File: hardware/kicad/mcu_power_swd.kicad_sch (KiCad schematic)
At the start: 27 parts, among them J1 5V INPUT: 1=+5V 2=GND, J2 SWD: VTref IO GND CLK RST SWO, U1 STM32G431RBT6, U2 AP2112K-3.3TRG1

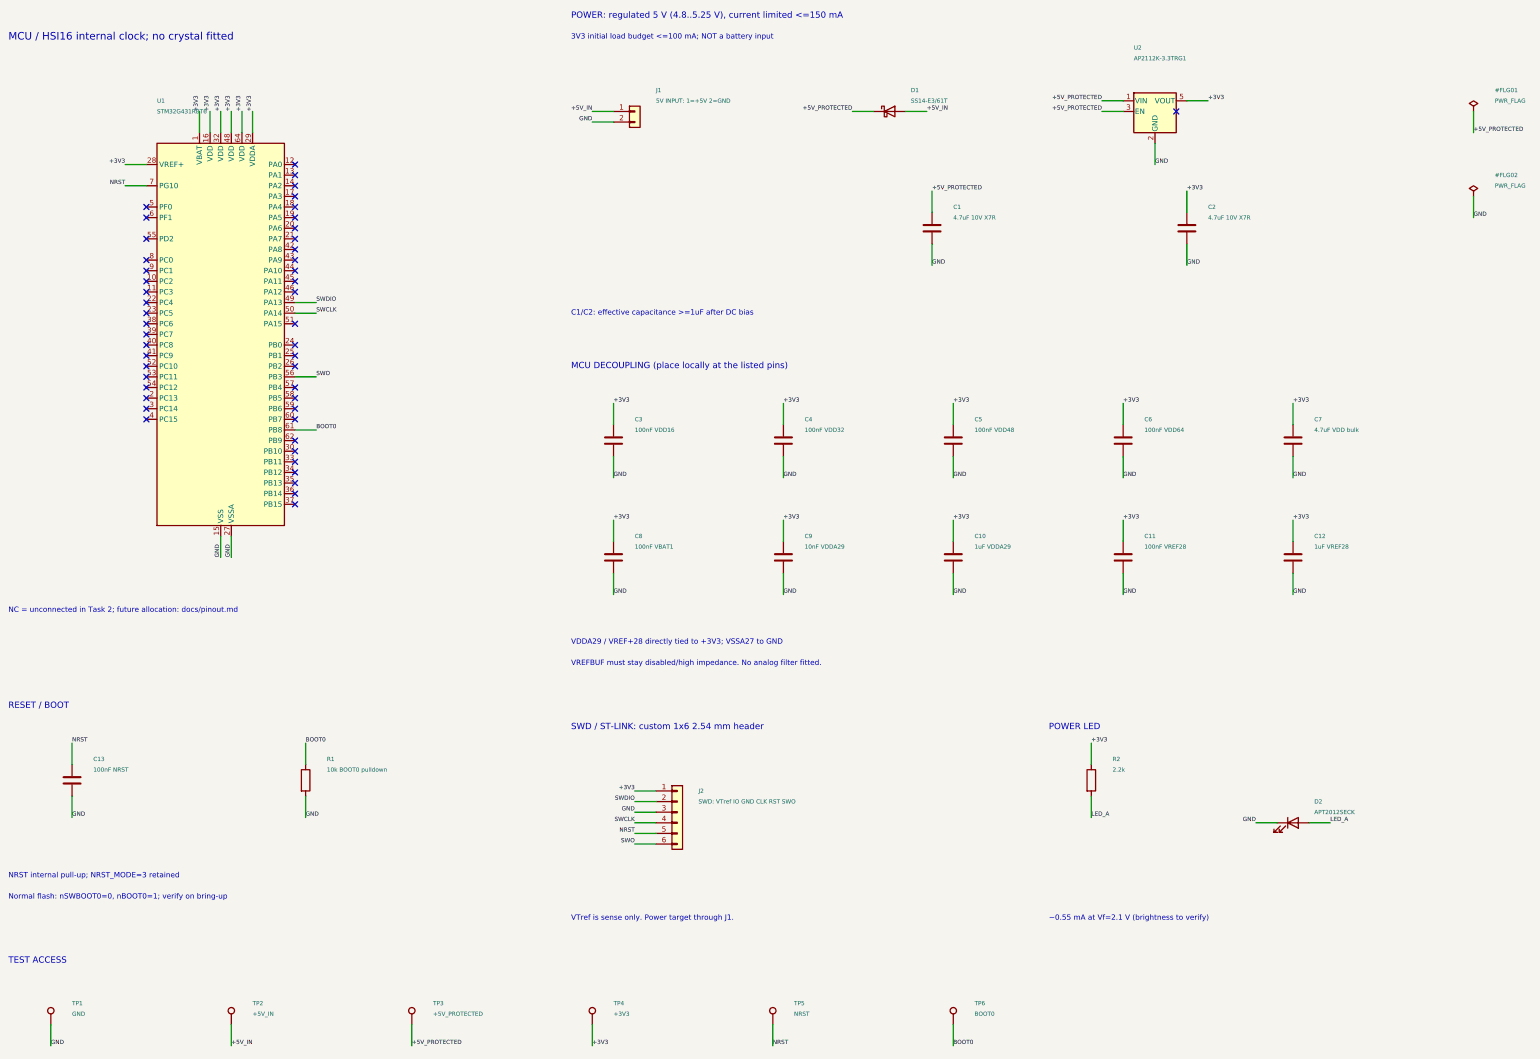
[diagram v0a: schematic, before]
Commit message: hardware: add verified CAN sensor and ESC interfaces
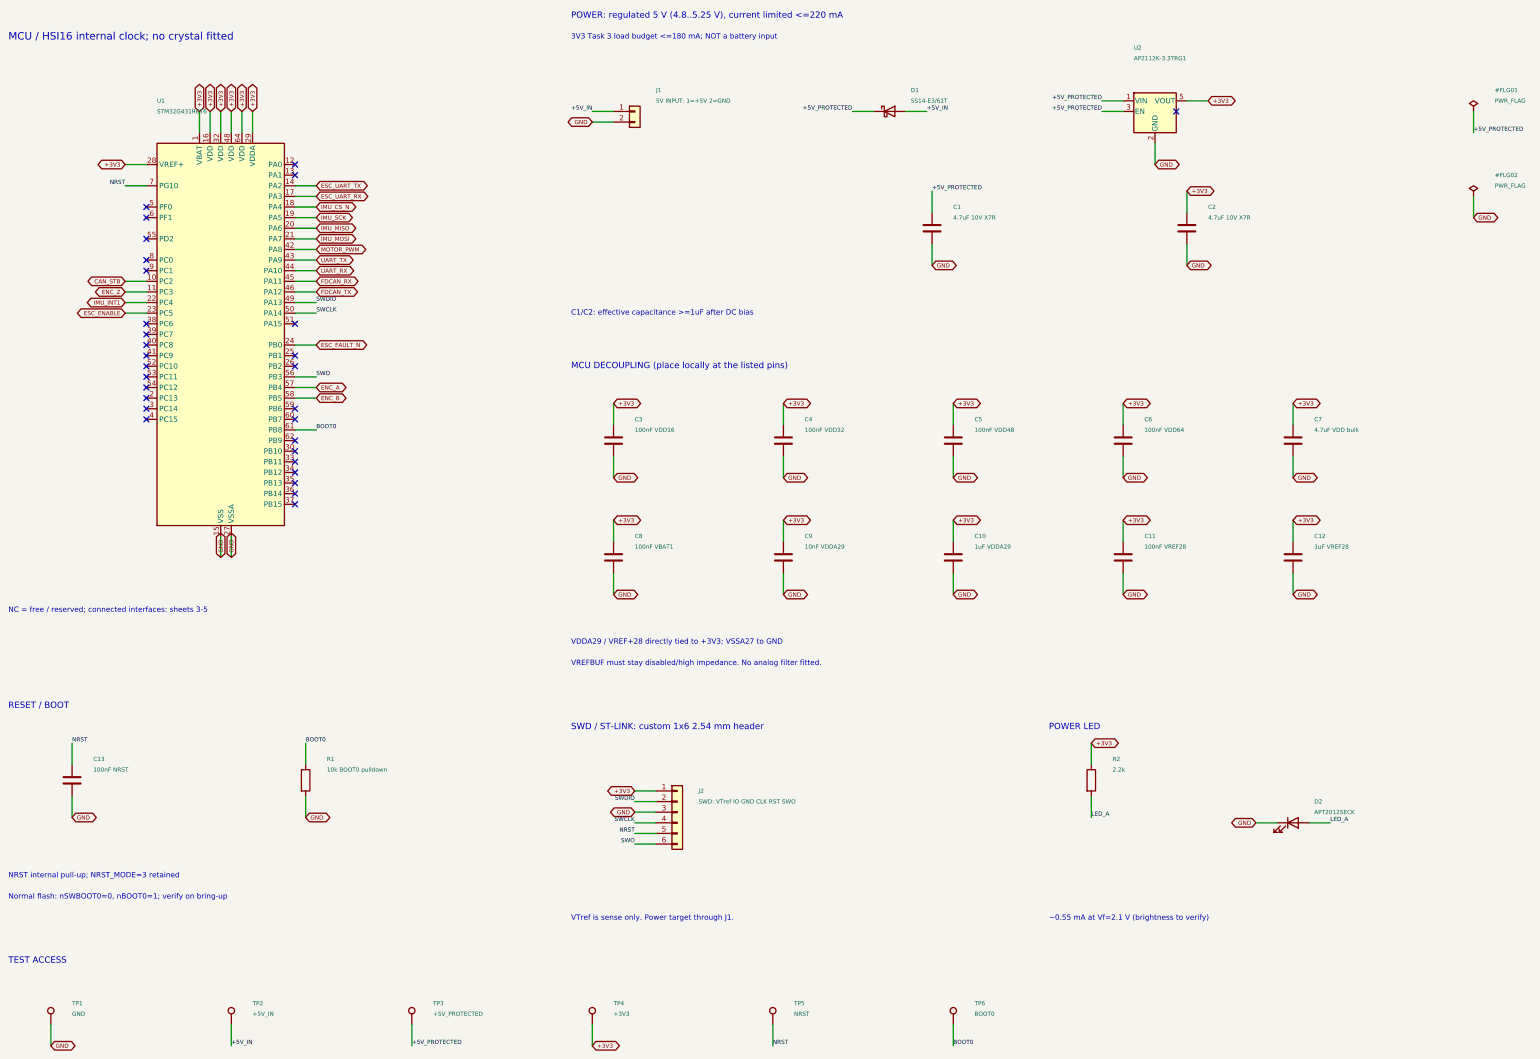
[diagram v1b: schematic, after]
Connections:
- net CAN_STB: now reaches U1.10 (PC2)
- net ENC_Z: now reaches U1.11 (PC3)
- net ESC_UART_TX: now reaches U1.14 (PA2)
- net ESC_UART_RX: now reaches U1.17 (PA3)
- net IMU_CS_N: now reaches U1.18 (PA4)
- net IMU_SCK: now reaches U1.19 (PA5)
- net IMU_MISO: now reaches U1.20 (PA6)
- net IMU_MOSI: now reaches U1.21 (PA7)
- net IMU_INT1: now reaches U1.22 (PC4)
- net ESC_ENABLE: now reaches U1.23 (PC5)
- net ESC_FAULT_N: now reaches U1.24 (PB0)
- net MOTOR_PWM: now reaches U1.42 (PA8)
- net UART_TX: now reaches U1.43 (PA9)
- net UART_RX: now reaches U1.44 (PA10)
- net FDCAN_RX: now reaches U1.45 (PA11)
- net FDCAN_TX: now reaches U1.46 (PA12)
- net ENC_A: now reaches U1.57 (PB4)
- net ENC_B: now reaches U1.58 (PB5)
- no-connect marks 48 -> 30
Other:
- note added: "3V3 Task 3 load budget <=180 mA; NOT a battery input"
- note added: "NC = free / reserved; connected interfaces: sheets 3-5"
- note added: "POWER: regulated 5 V (4.8..5.25 V), current limited <=220 mA"
- note removed: "3V3 initial load budget <=100 mA; NOT a battery input"
- note removed: "NC = unconnected in Task 2; future allocation: docs/pinout.md"
- note removed: "POWER: regulated 5 V (4.8..5.25 V), current limited <=150 mA"
- title: MCU + power + SWD - Task 2 -> MCU + power + SWD - Task 3 connections

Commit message: hardware: review schematic and align mechanical and probe attributes
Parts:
- TP1, TP2, TP3, TP4, TP5, TP6: now left out of the parts list
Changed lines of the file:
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@@
 (text "~0.55 mA at Vf=2.1 V (brightness to verify)" (at 274.32 241.3 0) (effects (font (size 1.27 1.27)) (justify left)))
 (text "TEST ACCESS" (at 25.4 251.46 0) (effects (font (size 1.5 1.5)) (justify left)))
-(symbol (lib_id "Connector:TestPoint") (at 35.56 266.7 0) (unit 1) (in_bom yes) (on_board yes) (dnp no) (property "Reference" "TP1" (at 40.64 261.62 0) (effects (font (size 1.0 1.0)) (justify left))) (property "Value" "GND" (at 40.64 264.15999999999997 0) (effects (font (size 1.0 1.0)) (justify left))) (property "Footprint" "TestPoint:TestPoint_Pad_D1.5mm" (at 35.56 266.7 0) (effects (font (size 1.27 1.27)) (hide yes))) (instances (project "reaction_wheel_controller" (path "/56c7795e-d739-4c45-a73e-6c5ecdfd94b9/87e1ebbe-146b-4e6f-b02d-98c3ee8c4d35" (reference "TP1") (unit 1)))))
+(symbol (lib_id "Connector:TestPoint") (at 35.56 266.7 0) (unit 1) (in_bom no) (on_board yes) (dnp no) (property "Reference" "TP1" (at 40.64 261.62 0) (effects (font (size 1.0 1.0)) (justify left))) (property "Value" "GND" (at 40.64 264.15999999999997 0) (effects (font (size 1.0 1.0)) (justify left))) (property "Footprint" "TestPoint:TestPoint_Pad_D1.5mm" (at 35.56 266.7 0) (effects (font (size 1.27 1.27)) (hide yes))) (instances (project "reaction_wheel_controller" (path "/56c7795e-d739-4c45-a73e-6c5ecdfd94b9/87e1ebbe-146b-4e6f-b02d-98c3ee8c4d35" (reference "TP1") (unit 1)))))
 (wire (pts (xy 35.56 266.7) (xy 35.56 271.78)) (stroke (width 0) (type default)))
 (global_label "GND" (shape bidirectional) (at 35.56 271.78 0) (effects (font (size 1.0 1.0)) (justify left bottom)))
-(symbol (lib_id "Connector:TestPoint") (at 78.74000000000001 266.7 0) (unit 1) (in_bom yes) (on_board yes) (dnp no) (property "Reference" "TP2" (at 83.82000000000001 261.62 0) (effects (font (size 1.0 1.0)) (justify left))) (property "Value" "+5V_IN" (at 83.82000000000001 264.15999999999997 0) (effects (font (size 1.0 1.0)) (justify left))) (property "Footprint" "TestPoint:TestPoint_Pad_D1.5mm" (at 78.74000000000001 266.7 0) (effects (font (size 1.27 1.27)) (hide yes))) (instances (project "reaction_wheel_controller" (path "/56c7795e-d739-4c45-a73e-6c5ecdfd94b9/87e1ebbe-146b-4e6f-b02d-98c3ee8c4d35" (reference "TP2") (unit 1)))))
+(symbol (lib_id "Connector:TestPoint") (at 78.74000000000001 266.7 0) (unit 1) (in_bom no) (on_board yes) (dnp no) (property "Reference" "TP2" (at 83.82000000000001 261.62 0) (effects (font (size 1.0 1.0)) (justify left))) (property "Value" "+5V_IN" (at 83.82000000000001 264.15999999999997 0) (effects (font (size 1.0 1.0)) (justify left))) (property "Footprint" "TestPoint:TestPoint_Pad_D1.5mm" (at 78.74000000000001 266.7 0) (effects (font (size 1.27 1.27)) (hide yes))) (instances (project "reaction_wheel_controller" (path "/56c7795e-d739-4c45-a73e-6c5ecdfd94b9/87e1ebbe-146b-4e6f-b02d-98c3ee8c4d35" (reference "TP2") (unit 1)))))
 (wire (pts (xy 78.74 266.7) (xy 78.74 271.78)) (stroke (width 0) (type default)))
 (label "+5V_IN" (at 78.74 271.78 0) (effects (font (size 1.0 1.0)) (justify left bottom)))
-(symbol (lib_id "Connector:TestPoint") (at 121.92 266.7 0) (unit 1) (in_bom yes) (on_board yes) (dnp no) (property "Reference" "TP3" (at 127.0 261.62 0) (effects (font (size 1.0 1.0)) (justify left))) (property "Value" "+5V_PROTECTED" (at 127.0 264.15999999999997 0) (effects (font (size 1.0 1.0)) (justify left))) (property "Footprint" "TestPoint:TestPoint_Pad_D1.5mm" (at 121.92 266.7 0) (effects (font (size 1.27 1.27)) (hide yes))) (instances (project "reaction_wheel_controller" (path "/56c7795e-d739-4c45-a73e-6c5ecdfd94b9/87e1ebbe-146b-4e6f-b02d-98c3ee8c4d35" (reference "TP3") (unit 1)))))
+(symbol (lib_id "Connector:TestPoint") (at 121.92 266.7 0) (unit 1) (in_bom no) (on_board yes) (dnp no) (property "Reference" "TP3" (at 127.0 261.62 0) (effects (font (size 1.0 1.0)) (justify left))) (property "Value" "+5V_PROTECTED" (at 127.0 264.15999999999997 0) (effects (font (size 1.0 1.0)) (justify left))) (property "Footprint" "TestPoint:TestPoint_Pad_D1.5mm" (at 121.92 266.7 0) (effects (font (size 1.27 1.27)) (hide yes))) (instances (project "reaction_wheel_controller" (path "/56c7795e-d739-4c45-a73e-6c5ecdfd94b9/87e1ebbe-146b-4e6f-b02d-98c3ee8c4d35" (reference "TP3") (unit 1)))))
 (wire (pts (xy 121.92 266.7) (xy 121.92 271.78)) (stroke (width 0) (type default)))
 (label "+5V_PROTECTED" (at 121.92 271.78 0) (effects (font (size 1.0 1.0)) (justify left bottom)))
-(symbol (lib_id "Connector:TestPoint") (at 165.1 266.7 0) (unit 1) (in_bom yes) (on_board yes) (dnp no) (property "Reference" "TP4" (at 170.18 261.62 0) (effects (font (size 1.0 1.0)) (justify left))) (property "Value" "+3V3" (at 170.18 264.15999999999997 0) (effects (font (size 1.0 1.0)) (justify left))) (property "Footprint" "TestPoint:TestPoint_Pad_D1.5mm" (at 165.1 266.7 0) (effects (font (size 1.27 1.27)) (hide yes))) (instances (project "reaction_wheel_controller" (path "/56c7795e-d739-4c45-a73e-6c5ecdfd94b9/87e1ebbe-146b-4e6f-b02d-98c3ee8c4d35" (reference "TP4") (unit 1)))))
+(symbol (lib_id "Connector:TestPoint") (at 165.1 266.7 0) (unit 1) (in_bom no) (on_board yes) (dnp no) (property "Reference" "TP4" (at 170.18 261.62 0) (effects (font (size 1.0 1.0)) (justify left))) (property "Value" "+3V3" (at 170.18 264.15999999999997 0) (effects (font (size 1.0 1.0)) (justify left))) (property "Footprint" "TestPoint:TestPoint_Pad_D1.5mm" (at 165.1 266.7 0) (effects (font (size 1.27 1.27)) (hide yes))) (instances (project "reaction_wheel_controller" (path "/56c7795e-d739-4c45-a73e-6c5ecdfd94b9/87e1ebbe-146b-4e6f-b02d-98c3ee8c4d35" (reference "TP4") (unit 1)))))
 (wire (pts (xy 165.1 266.7) (xy 165.1 271.78)) (stroke (width 0) (type default)))
 (global_label "+3V3" (shape bidirectional) (at 165.1 271.78 0) (effects (font (size 1.0 1.0)) (justify left bottom)))
-(symbol (lib_id "Connector:TestPoint") (at 208.28 266.7 0) (unit 1) (in_bom yes) (on_board yes) (dnp no) (property "Reference" "TP5" (at 213.36 261.62 0) (effects (font (size 1.0 1.0)) (justify left))) (property "Value" "NRST" (at 213.36 264.15999999999997 0) (effects (font (size 1.0 1.0)) (justify left))) (property "Footprint" "TestPoint:TestPoint_Pad_D1.5mm" (at 208.28 266.7 0) (effects (font (size 1.27 1.27)) (hide yes))) (instances (project "reaction_wheel_controller" (path "/56c7795e-d739-4c45-a73e-6c5ecdfd94b9/87e1ebbe-146b-4e6f-b02d-98c3ee8c4d35" (reference "TP5") (unit 1)))))
+(symbol (lib_id "Connector:TestPoint") (at 208.28 266.7 0) (unit 1) (in_bom no) (on_board yes) (dnp no) (property "Reference" "TP5" (at 213.36 261.62 0) (effects (font (size 1.0 1.0)) (justify left))) (property "Value" "NRST" (at 213.36 264.15999999999997 0) (effects (font (size 1.0 1.0)) (justify left))) (property "Footprint" "TestPoint:TestPoint_Pad_D1.5mm" (at 208.28 266.7 0) (effects (font (size 1.27 1.27)) (hide yes))) (instances (project "reaction_wheel_controller" (path "/56c7795e-d739-4c45-a73e-6c5ecdfd94b9/87e1ebbe-146b-4e6f-b02d-98c3ee8c4d35" (reference "TP5") (unit 1)))))
 (wire (pts (xy 208.28 266.7) (xy 208.28 271.78)) (stroke (width 0) (type default)))
 (label "NRST" (at 208.28 271.78 0) (effects (font (size 1.0 1.0)) (justify left bottom)))
-(symbol (lib_id "Connector:TestPoint") (at 251.46 266.7 0) (unit 1) (in_bom yes) (on_board yes) (dnp no) (property "Reference" "TP6" (at 256.54 261.62 0) (effects (font (size 1.0 1.0)) (justify left))) (property "Value" "BOOT0" (at 256.54 264.15999999999997 0) (effects (font (size 1.0 1.0)) (justify left))) (property "Footprint" "TestPoint:TestPoint_Pad_D1.5mm" (at 251.46 266.7 0) (effects (font (size 1.27 1.27)) (hide yes))) (instances (project "reaction_wheel_controller" (path "/56c7795e-d739-4c45-a73e-6c5ecdfd94b9/87e1ebbe-146b-4e6f-b02d-98c3ee8c4d35" (reference "TP6") (unit 1)))))
+(symbol (lib_id "Connector:TestPoint") (at 251.46 266.7 0) (unit 1) (in_bom no) (on_board yes) (dnp no) (property "Reference" "TP6" (at 256.54 261.62 0) (effects (font (size 1.0 1.0)) (justify left))) (property "Value" "BOOT0" (at 256.54 264.15999999999997 0) (effects (font (size 1.0 1.0)) (justify left))) (property "Footprint" "TestPoint:TestPoint_Pad_D1.5mm" (at 251.46 266.7 0) (effects (font (size 1.27 1.27)) (hide yes))) (instances (project "reaction_wheel_controller" (path "/56c7795e-d739-4c45-a73e-6c5ecdfd94b9/87e1ebbe-146b-4e6f-b02d-98c3ee8c4d35" (reference "TP6") (unit 1)))))
 (wire (pts (xy 251.46 266.7) (xy 251.46 271.78)) (stroke (width 0) (type default)))
 (label "BOOT0" (at 251.46 271.78 0) (effects (font (size 1.0 1.0)) (justify left bottom)))
